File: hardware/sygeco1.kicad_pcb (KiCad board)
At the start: 2 copper layers, 30.5 x 73 mm, 16 parts, among them J1 SSD1306_module, J2 AVR-ISP-6, SW1 SW_Push_DPDT, SW2 SW_Push_DPDT, U1 ATtiny85-20PU

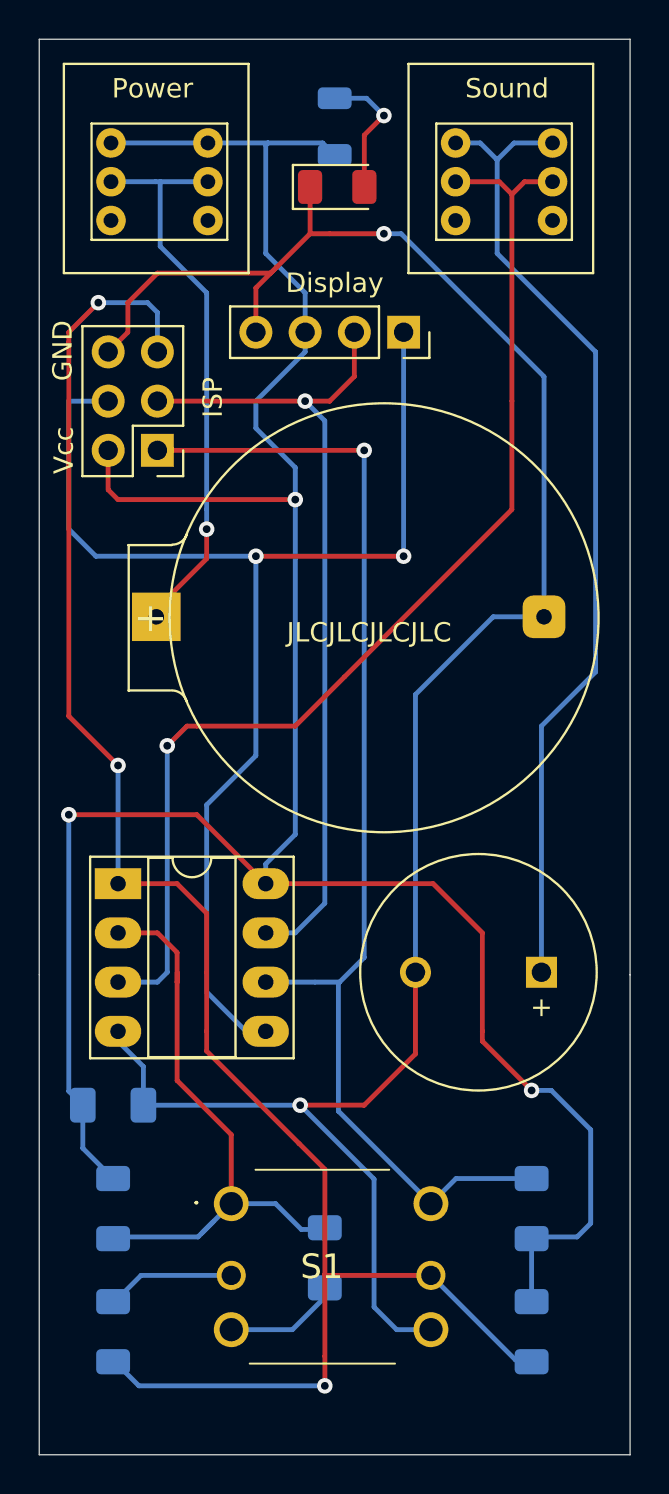
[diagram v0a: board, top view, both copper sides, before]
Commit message: add mounting holes for the screen
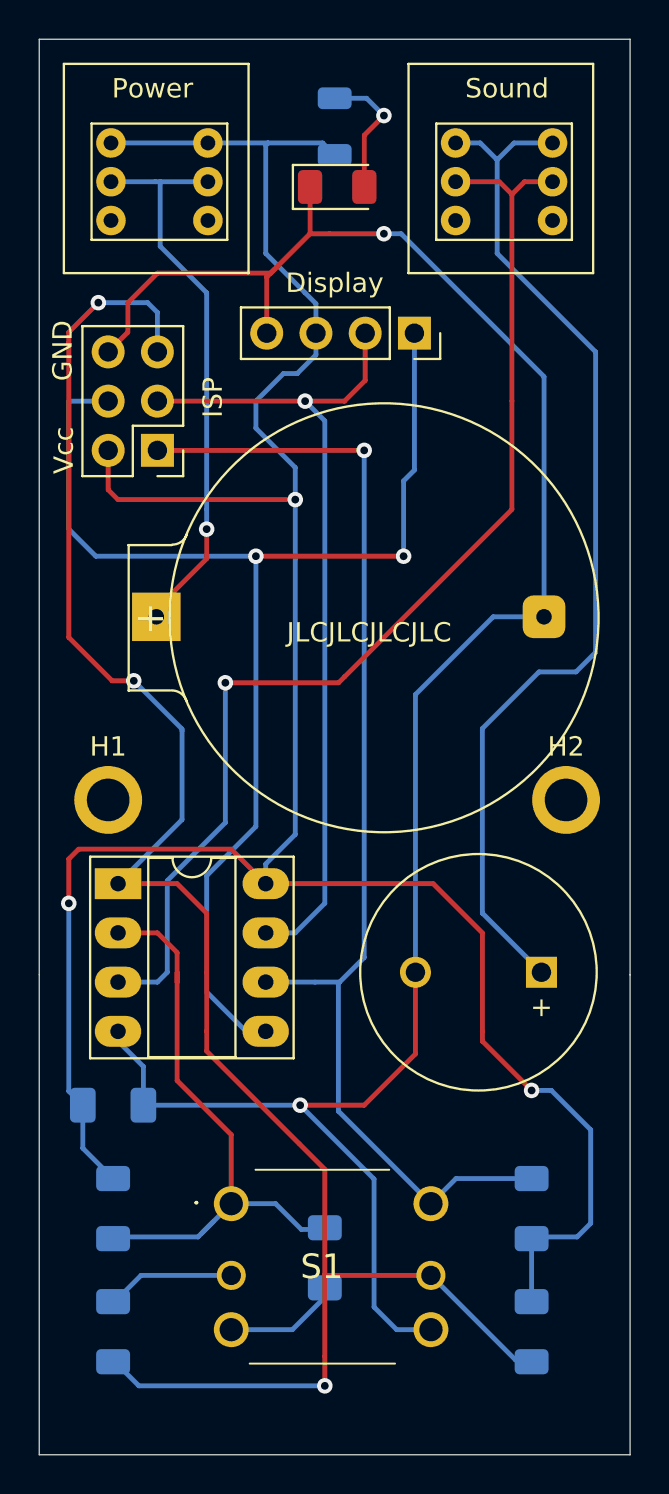
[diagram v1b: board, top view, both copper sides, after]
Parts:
- added H1: MountingHole, MountingHole:MountingHole_2.2mm_M2_ISO7380_Pad, F.Cu at (130.6, 93.2)
- added H2: MountingHole, MountingHole:MountingHole_2.2mm_M2_ISO7380_Pad, F.Cu at (154.2, 93.2)
- moved J1 0.56 mm to (146.4, 69.1)
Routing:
- net Net-(LS1-Pad1): track 50.9 -> 54.5 mm
- net PAD_AXIS_1: track 93.0 -> 96.4 mm
- net VCC: track 133.6 -> 131.6 mm
- net SCL: track 43.0 -> 43.6 mm

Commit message: Restore original (tinyjoypad) input schematics, with dual resistors and reset pin >= vcc/2
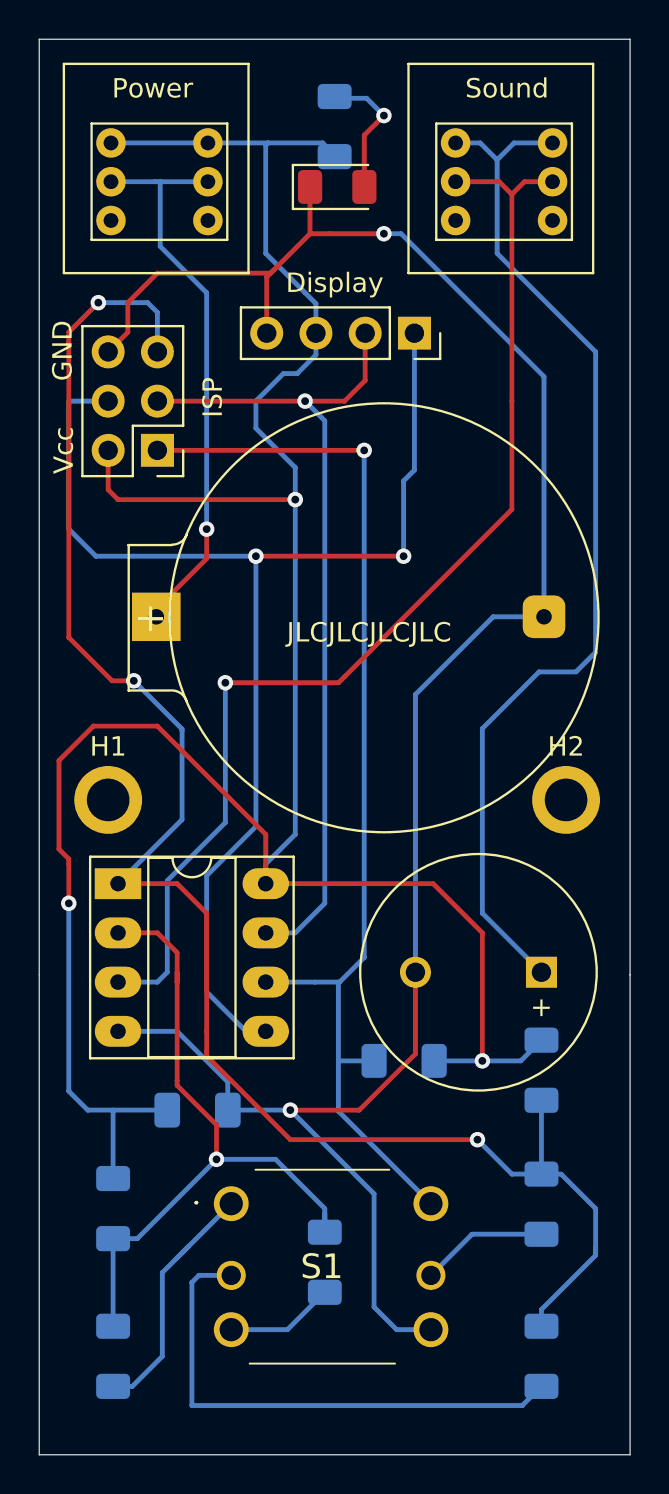
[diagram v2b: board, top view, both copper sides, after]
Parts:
- added R7: 22k, Resistor_SMD:R_1206_3216Metric_Pad1.30x1.75mm_HandSolder, B.Cu at (152.9, 107.2)
- added R8: 88k, Resistor_SMD:R_1206_3216Metric_Pad1.30x1.75mm_HandSolder, B.Cu at (152.9, 121.9)
- R1, R2: value 50k -> 33k
- R4: value 50k -> 22k
- R5: value 50k -> 88k
- R6: footprint Resistor_SMD:R_1206_3216Metric -> Resistor_SMD:R_1206_3216Metric_Pad1.30x1.75mm_HandSolder
- moved R2 23.1 mm to (152.9, 114.1), turned to 270 degrees
- moved R1 21.6 mm to (130.8, 121.9)
- moved R3 10.1 mm to (145.8, 106.7), turned to 180 degrees
- moved C1 4.36 mm to (135.2, 109.2)
- moved R5 0.23 mm to (141.7, 117.1)
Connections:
- R1 pad 1: VCC -> PAD_AXIS_2
- R1 pad 2: PAD_AXIS_1 -> Net-(R1-Pad2)
- S1 pad 1: PAD_AXIS_2 -> Net-(R1-Pad2)
- S1 pad 2: Net-(R2-Pad2) -> Net-(R8-Pad2)
- S1 pad 5: PAD_AXIS_1 -> Net-(R2-Pad2)
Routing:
- net Net-(R8-Pad2): track 0.00 -> 27.5 mm
- net Net-(R1-Pad2): track 0.00 -> 13.3 mm
- net PAD_AXIS_1: track 96.4 -> 87.5 mm
- net PAD_AXIS_2: track 32.1 -> 37.4 mm, vias 0 -> 1
- net Button: track 61.6 -> 57.7 mm
- net VCC: track 131.6 -> 133.5 mm
- net Net-(R2-Pad2): track 7.26 -> 6.58 mm

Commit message: Add a led to provide feedback about whether the sound is enable or not.
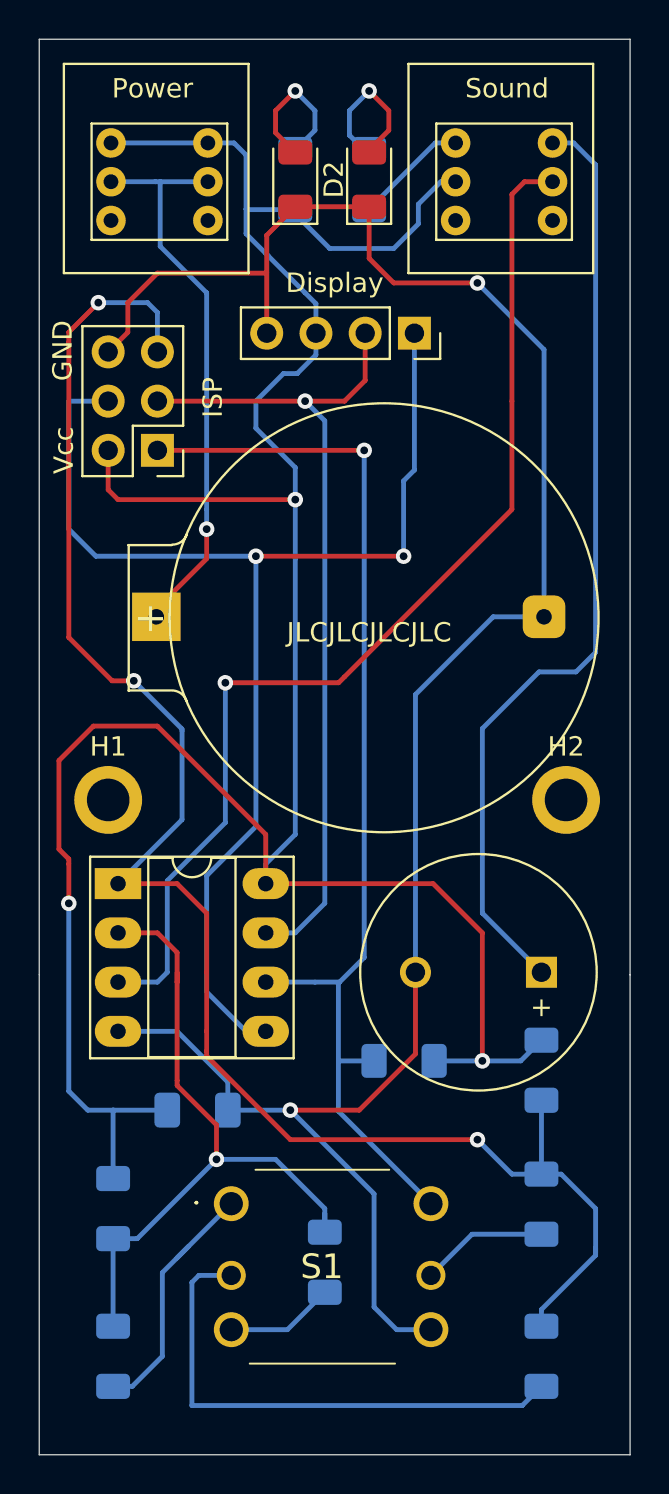
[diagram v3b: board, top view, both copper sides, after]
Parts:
- added D2: LED, LED_SMD:LED_1206_3216Metric, F.Cu at (144.0, 61.2)
- added R9: 150, Resistor_SMD:R_1206_3216Metric_Pad1.30x1.75mm_HandSolder, B.Cu at (144.0, 61.2)
- R6: value 60~100 -> 150
- moved R6 3.41 mm to (140.2, 61.2)
- moved D1 2.20 mm to (140.2, 61.2), turned to 90 degrees
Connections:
- SW2 pad 2: Net-(SW2-Pad2) -> VCC
- SW2 pad 3: Net-(LS1-Pad1) -> Net-(R9-Pad1)
- SW2 pad 5: Net-(SW2-Pad2) -> Net-(SW2-Pad5)
- U1 pad 3: Net-(SW2-Pad2) -> Net-(SW2-Pad5)
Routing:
- net Net-(SW2-Pad2): track 59.2 -> 0.00 mm, vias 1 -> 0
- net Net-(SW2-Pad5): track 0.00 -> 56.0 mm, vias 0 -> 1
- net VCC: track 133.5 -> 142.7 mm
- net Net-(D2-Pad2): track 0.00 -> 8.05 mm, vias 0 -> 1
- net Net-(R9-Pad1): track 0.00 -> 5.90 mm
- net Net-(LS1-Pad1): track 54.5 -> 49.1 mm
- net GND: track 108.7 -> 110.7 mm
- net Net-(D1-Pad2): track 7.01 -> 8.28 mm

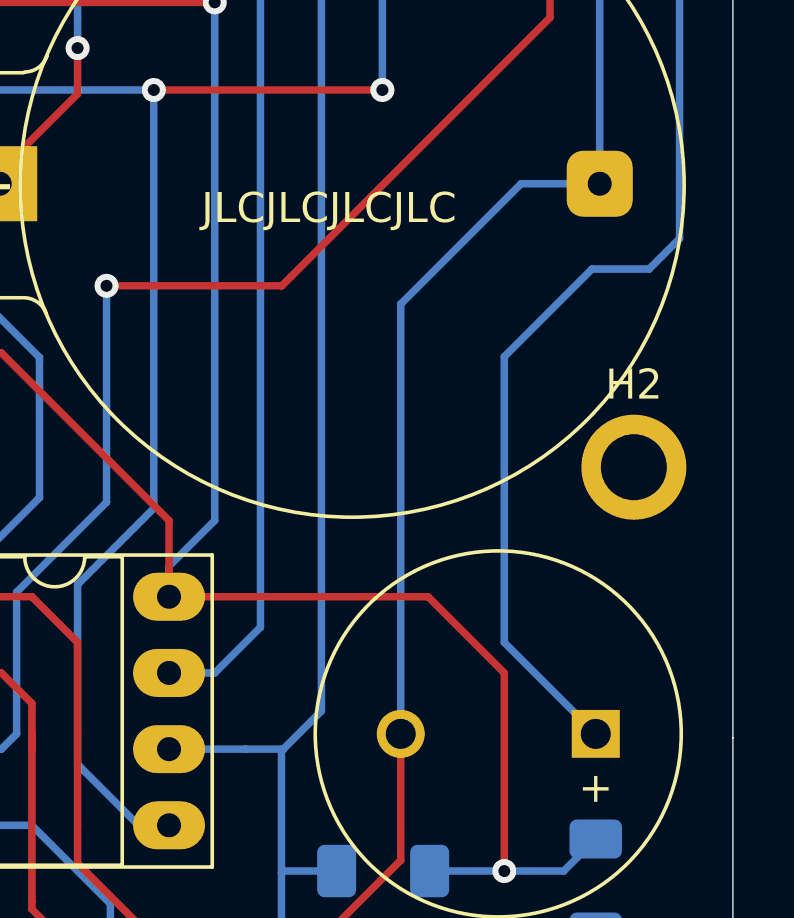
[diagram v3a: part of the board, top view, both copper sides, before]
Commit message: Add a resistor to lower the level of buzzer (especially when using li-ion battery, with higher voltage) + fixes leds resistors.
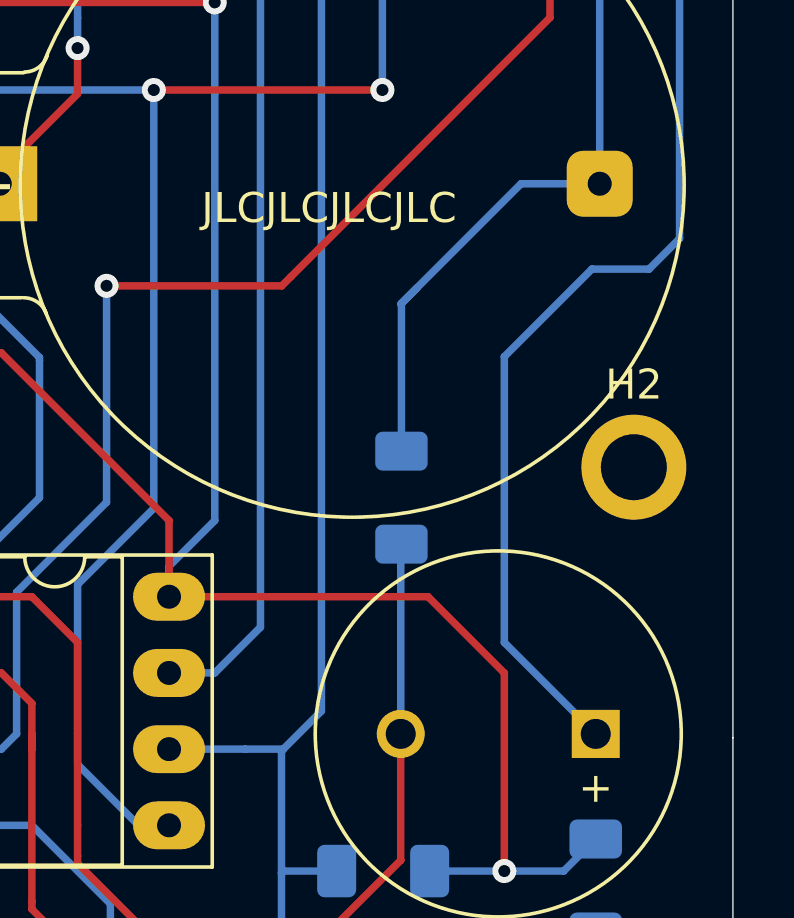
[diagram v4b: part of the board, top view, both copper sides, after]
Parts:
- added R10: 220, Resistor_SMD:R_1206_3216Metric_Pad1.30x1.75mm_HandSolder, B.Cu at (146.4, 94.2)
- R6, R9: value 150 -> 470
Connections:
- LS1 pad 2: GND -> Net-(LS1-Pad2)
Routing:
- net GND: track 110.7 -> 102.0 mm
- net Net-(LS1-Pad2): track 0.00 -> 6.33 mm

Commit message: cleaning
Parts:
- added G***: LOGO, sygeco:Sylphide_logo, F.Cu at (152.8, 117.2)
- added REF**: OSHW-Logo2_7.3x6mm_SilkScreen, Symbol:OSHW-Logo2_7.3x6mm_SilkScreen, F.Cu at (132.0, 117.0)
- moved R10 3.26 mm to (149.3, 92.7)
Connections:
- LS1 pad 2: Net-(LS1-Pad2) -> GND
- R10 pad 1: Net-(LS1-Pad2) -> Net-(LS1-Pad1)
- R10 pad 2: GND -> Net-(R10-Pad2)
- SW2 pad 6: Net-(LS1-Pad1) -> Net-(R10-Pad2)
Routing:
- net Net-(R10-Pad2): track 0.00 -> 40.6 mm
- net Net-(LS1-Pad1): track 49.1 -> 9.38 mm
- net GND: track 102.0 -> 114.9 mm
- net Net-(LS1-Pad2): track 6.33 -> 0.00 mm
- net SDA: track 65.6 -> 70.9 mm, vias 2 -> 1
- net PAD_AXIS_1: track 87.5 -> 88.4 mm
- net VCC: track 142.7 -> 142.1 mm
- net Net-(BT1-Pad1): vias 1 -> 0

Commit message: final touch + generates files for pcb production
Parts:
- R3: value 50k -> 10k
